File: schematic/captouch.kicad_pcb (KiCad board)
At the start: 2 copper layers, 30 x 50 mm, 14 parts, among them P1 CONN_01X02, P2 CONN_01X04, P3 CONN_01X03, Q1 DMN3404L, U1 LD1117S33CTR, U2 MSP430G2553IPW20

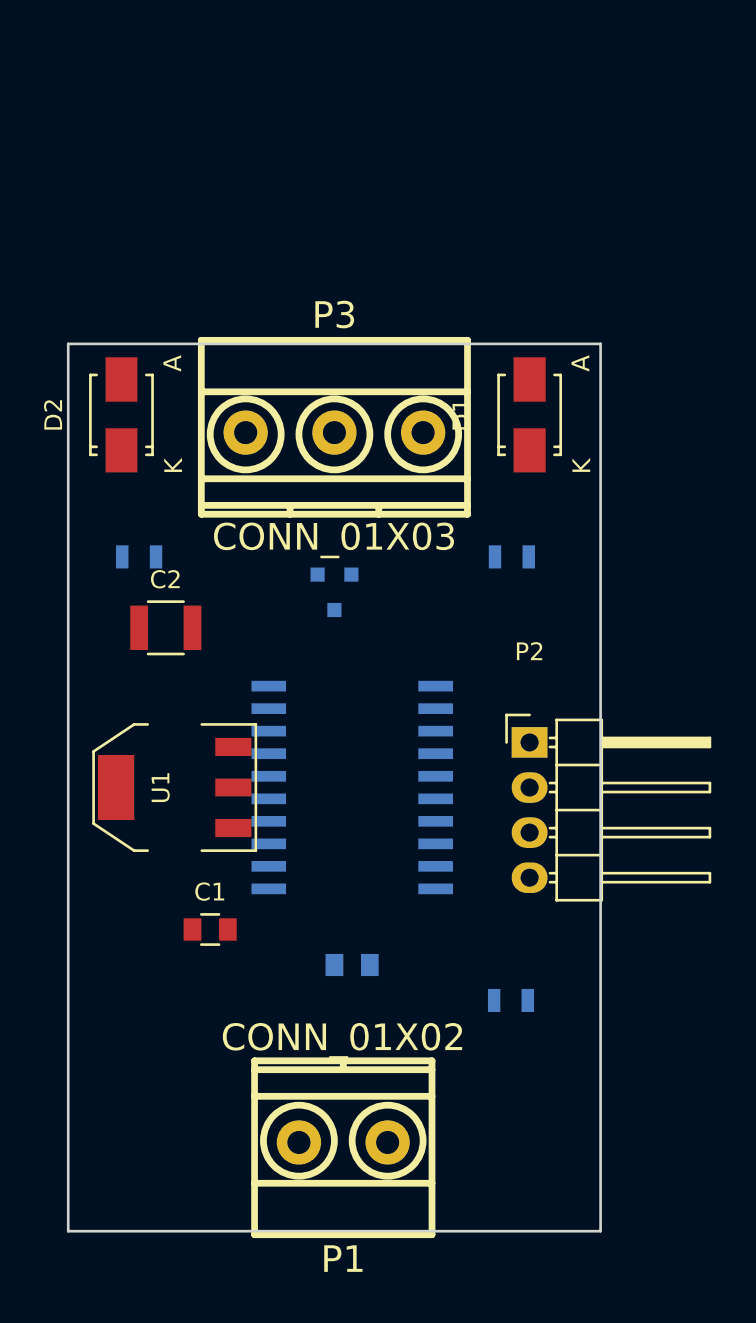
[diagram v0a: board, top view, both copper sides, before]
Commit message: Started layout
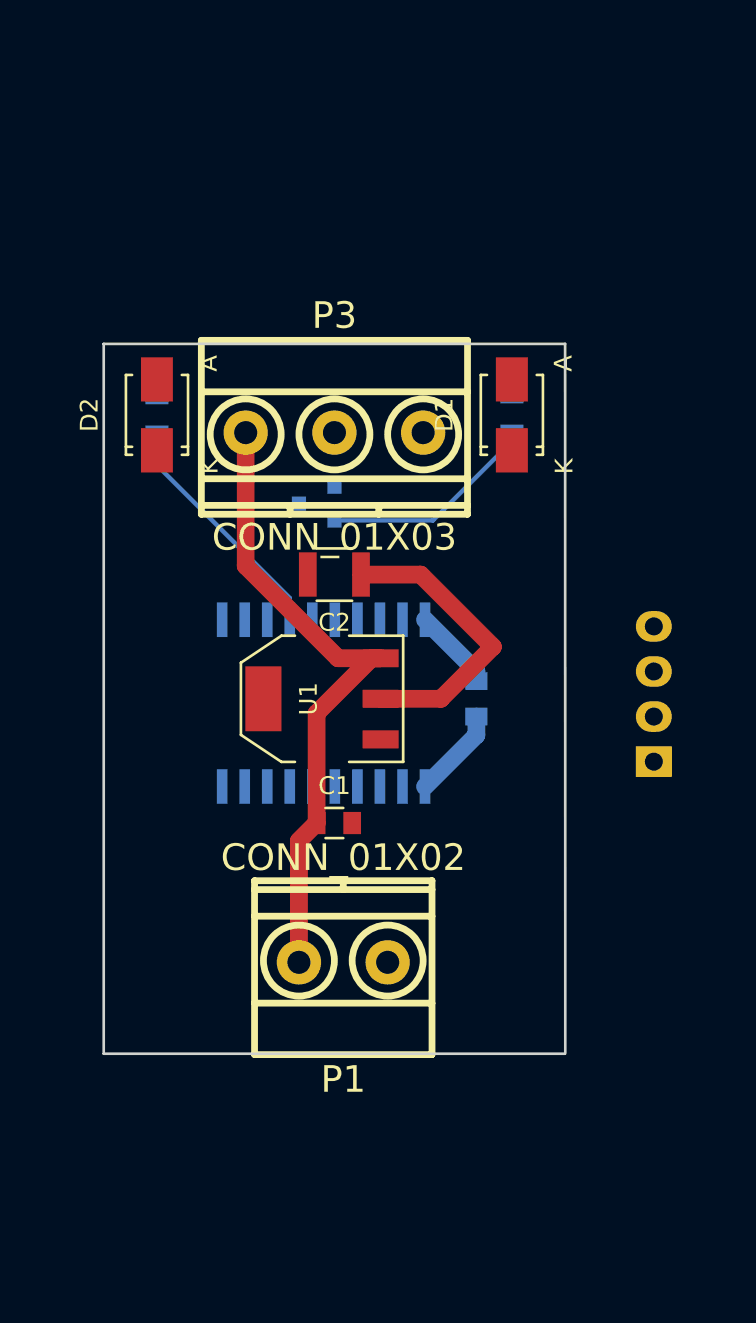
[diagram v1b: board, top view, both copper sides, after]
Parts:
- removed R1: 47k, Resistors_SMD:R_0805
- P2: moved to B.Cu
- moved C3 16.6 mm to (73.0, 55.0), turned to 90 degrees
- moved P1 10.2 mm to (65.5, 69.8)
- moved C2 9.96 mm to (65.0, 48.0), turned to 180 degrees
- moved U1 9.69 mm to (64.3, 55.0)
- moved C1 9.22 mm to (65.0, 62.0)
- moved R3 8.06 mm to (55.0, 39.0), turned to 270 degrees
- moved R2 8.05 mm to (75.0, 39.0), turned to 270 degrees
- moved P2 7.08 mm to (83.0, 58.5)
- moved Q1 5.10 mm to (64.0, 44.0), turned to 270 degrees
- moved U2 5.02 mm to (64.4, 55.2), turned to 90 degrees
- moved D2 2.00 mm to (55.0, 39.0)
- moved D1 1.00 mm to (75.0, 39.0)
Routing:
- net Net-(C1-Pad1): track 0.00 -> 36.6 mm
- net +3V3: track 0.00 -> 22.3 mm
- net Net-(R3-Pad2): track 0.00 -> 13.7 mm
- net Net-(Q1-Pad2): track 0.00 -> 12.4 mm
- net GNDREF: track 0.00 -> 4.65 mm
- net TEST: track 0.00 -> 0.67 mm
- net /RST: track 0.00 -> 0.67 mm
- added copper zone on F.Cu, net GNDREF
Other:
- board size 30 x 50 mm -> 26 x 40 mm
- net class Power added: clearance 0.2, trace_width 1, via_dia 2, via_drill 1

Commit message: Finished routing
Artwork is next
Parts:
- added R1: 47k, Resistors_SMD:R_0805, F.Cu at (72.9, 55.0)
- P1: value CONN_01X02 -> POWER
- P2: value CONN_01X04 -> PROG; moved to F.Cu
- P3: value CONN_01X03 -> LAMP
- moved C3 17.0 mm to (56.0, 55.0), turned to 270 degrees
- moved P2 9.63 mm to (76.0, 51.9)
- moved C2 2.61 mm to (67.5, 47.2)
- moved C1 2.50 mm to (67.5, 62.0)
- moved P1 0.52 mm to (65.0, 70.0), turned to 0 degrees
- moved Q1 0.25 mm to (64.0, 44.2)
- turned P3 to 180 degrees
- turned U2 to 270 degrees
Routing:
- net +3V3: track 22.3 -> 47.1 mm
- net Net-(R3-Pad2): track 13.7 -> 33.1 mm
- net Net-(P3-Pad3): track 0.00 -> 16.7 mm
- net /RST: track 0.67 -> 17.4 mm
- net TEST: track 0.67 -> 16.2 mm
- net Net-(Q1-Pad2): track 12.4 -> 22.4 mm, vias 0 -> 2
- net Net-(C1-Pad1): track 36.6 -> 32.9 mm
- net Net-(P3-Pad2): track 0.00 -> 3.30 mm
- net Net-(D2-Pad2): track 0.00 -> 3.05 mm, vias 0 -> 1
- net Net-(D1-Pad2): track 0.00 -> 3.00 mm, vias 0 -> 1
- net GNDREF: track 4.65 -> 7.32 mm, vias 0 -> 2
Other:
- board text added: "S"

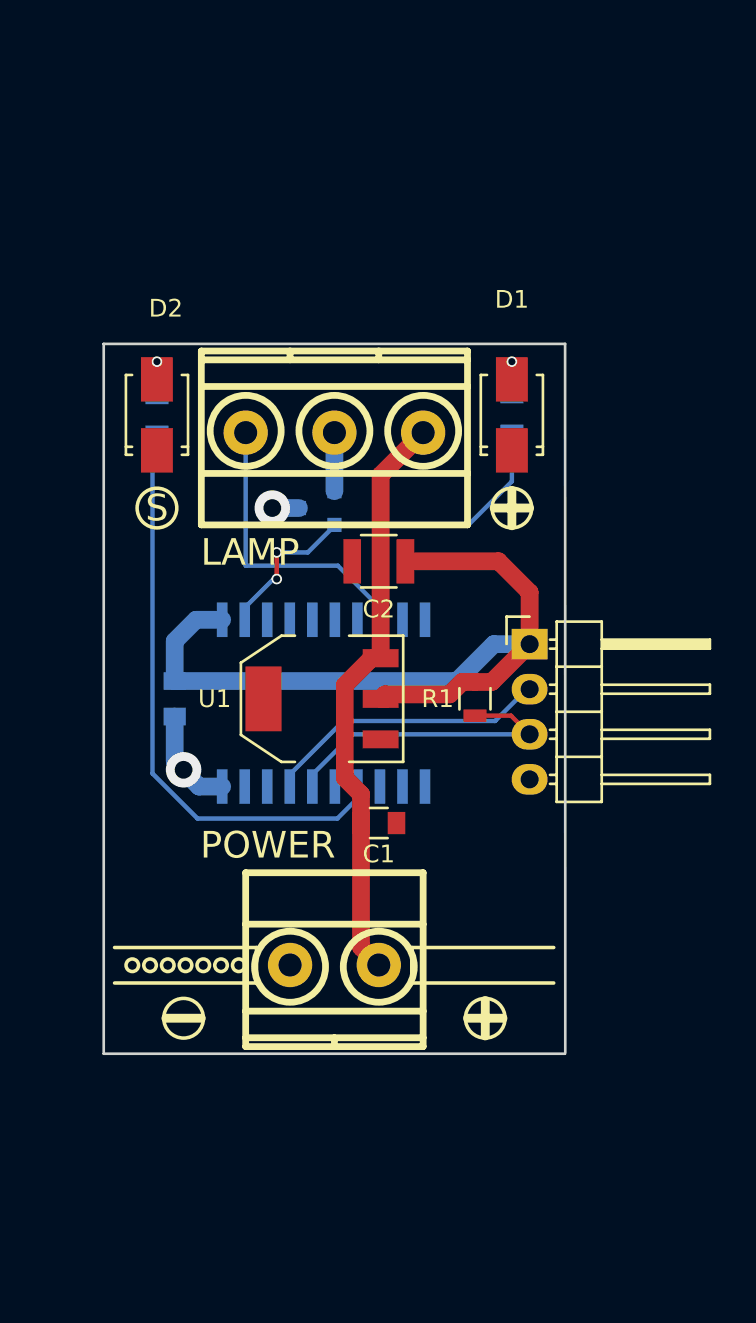
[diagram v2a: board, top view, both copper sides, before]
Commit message: Added logos
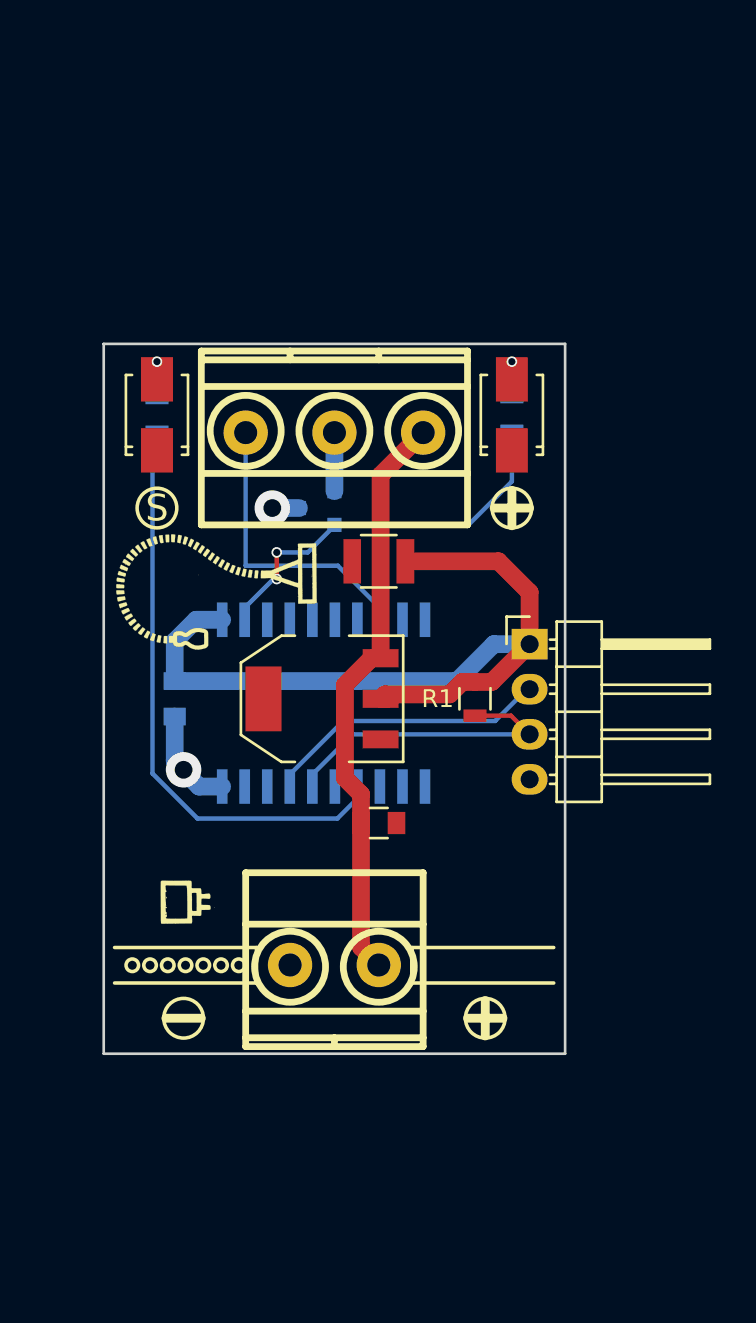
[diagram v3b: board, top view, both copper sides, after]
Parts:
- added G***: LOGO, logo:lamp, F.Cu at (58.5, 48.8)
- added G***: LOGO, logo:plug, F.Cu at (56.5, 65.5)
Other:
- outline, holes or cut-outs redrawn
- board text added: "Captouch Lamp Switch"
- board text added: "WPD 201605"

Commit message: Incorporated Martins schematic comments
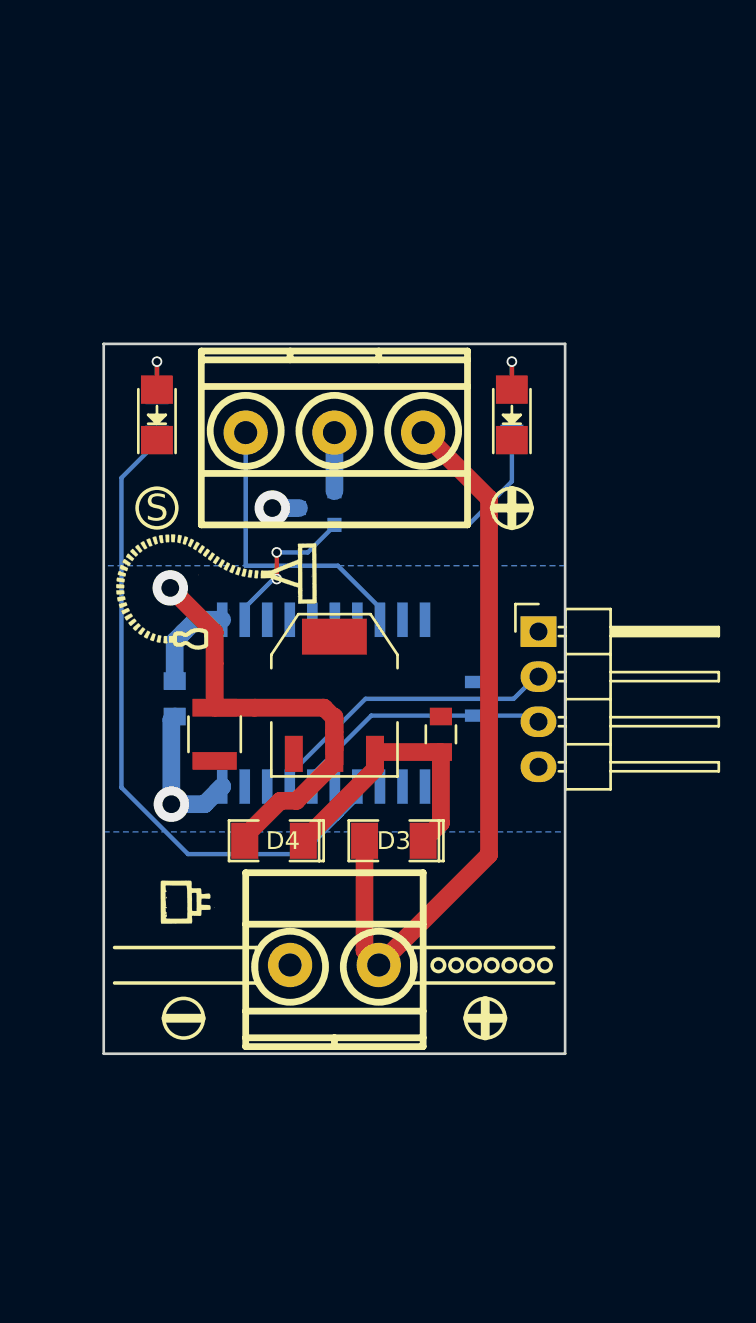
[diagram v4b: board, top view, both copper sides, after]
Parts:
- added D3: D, SMD_Packages:SMD-1206_Pol, F.Cu at (68.3, 63.0)
- added D4: D, SMD_Packages:SMD-1206_Pol, F.Cu at (61.6, 63.0)
- C3: value 1n -> 100n
- D1, D2: footprint Diodes_SMD:SMA_Standard -> LEDs:LED_1206
- P2: value PROG -> PROGRAM
- R1: moved to B.Cu
- moved C2 13.4 mm to (58.2, 57.0), turned to 270 degrees
- moved C1 6.10 mm to (71.0, 57.0), turned to 90 degrees
- moved P2 0.87 mm to (76.5, 51.2)
- moved U1 0.73 mm to (65.0, 54.8), turned to 0 degrees
- moved R1 0.08 mm to (73.0, 55.0)
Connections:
- P1 pad 2: Net-(C1-Pad1) -> Net-(D3-Pad2)
- P3 pad 1: Net-(C1-Pad1) -> Net-(D3-Pad2)
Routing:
- net Net-(D3-Pad2): track 0.00 -> 41.4 mm
- net Net-(C1-Pad1): track 32.9 -> 14.9 mm
- net +3V3: track 47.1 -> 31.7 mm, vias 0 -> 1
- net Net-(R3-Pad2): track 33.1 -> 38.7 mm
- net GNDREF: track 7.32 -> 10.2 mm
- net /RST: track 17.4 -> 14.9 mm
- net TEST: track 16.2 -> 17.0 mm
- net Net-(P3-Pad3): track 16.7 -> 16.0 mm
- added copper zone on B.Cu, net +3V3

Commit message: More little adjustments + logo
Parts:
- removed G***: LOGO, logo:lamp
- added ?: , logo:lamp, F.Cu at (58.5, 32.8)
- added ?: , logo:wpd, B.Cu at (56.0, 54.0)
- ?: renamed from G***; value LOGO -> (none)
- P1: footprint w_conn_mkds:mkds_1,5-2 -> conn:P_1,5-2
- P2: footprint Pin_Headers:Pin_Header_Angled_1x04 -> Pin_Headers:Pin_Header_Angled_1x06; moved to B.Cu
- P3: footprint w_conn_mkds:mkds_1,5-3 -> conn:P_1,5-3
- U2: footprint Housings_SOIC:SOIC-20_7.5x12.8mm_Pitch1.27mm -> Housings_SSOP:TSSOP-20_4.4x6.5mm_Pitch0.65mm
- moved P3 16.8 mm to (65.0, 23.2)
- moved C3 16.4 mm to (59.5, 39.0)
- moved U2 16.3 mm to (64.8, 39.0)
- moved C1 16.0 mm to (70.2, 41.0)
- moved C2 16.0 mm to (59.0, 41.0)
- moved R2 16.0 mm to (75.0, 22.9)
- moved D1 16.0 mm to (75.0, 23.0)
- moved D2 16.0 mm to (55.0, 23.0)
- moved D3 16.0 mm to (68.3, 47.0)
- moved D4 16.0 mm to (61.6, 47.0)
- moved Q1 16.0 mm to (64.0, 28.2)
- moved R3 16.0 mm to (55.0, 23.0)
- moved U1 16.0 mm to (65.0, 38.8)
- moved ? 15.5 mm to (56.5, 50.0)
- moved P1 15.5 mm to (65.0, 54.5)
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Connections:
- P2 pad 4: GNDREF -> RXD
- U2 pad 3: (no net) -> TXD
- U2 pad 4: (no net) -> RXD
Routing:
- net +3V3: track 31.7 -> 57.1 mm, vias 1 -> 2
- net TXD: track 0.00 -> 17.8 mm, vias 0 -> 1
- net RXD: track 0.00 -> 14.6 mm
- net Net-(P3-Pad3): track 16.0 -> 19.1 mm
- net Net-(P3-Pad2): track 3.30 -> 5.30 mm
- net /RST: track 14.9 -> 16.7 mm
- net Net-(D3-Pad2): track 41.4 -> 43.1 mm
- net GNDREF: track 10.2 -> 11.8 mm
- net Net-(C1-Pad1): track 14.9 -> 13.8 mm
- net Net-(R3-Pad2): track 38.7 -> 38.1 mm
- net TEST: track 17.0 -> 16.8 mm, vias 0 -> 1
- removed copper zone on B.Cu, net +3V3
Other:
- board text added: "201605"
- board text added: "3V3"
- board text added: "GND"
- board text added: "RST"
- board text added: "RX"
- board text added: "TST"
- board text added: "TX"
- board text removed: "WPD 201605"
